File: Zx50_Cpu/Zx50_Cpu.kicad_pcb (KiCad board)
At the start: 4 copper layers, 139.2 x 100.3 mm, 24 parts, among them J1 Zx50_EdgeConnector, J2 FrontPanelConnect, J3 Clock Mezzanine, J4 Front Panel, SW1 RESET, U1 74AHC1G14, U2 SN74AHCT245N, U3 SN74AHCT245N, U4 Z84C00xxP, U5 SN74AHCT245N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

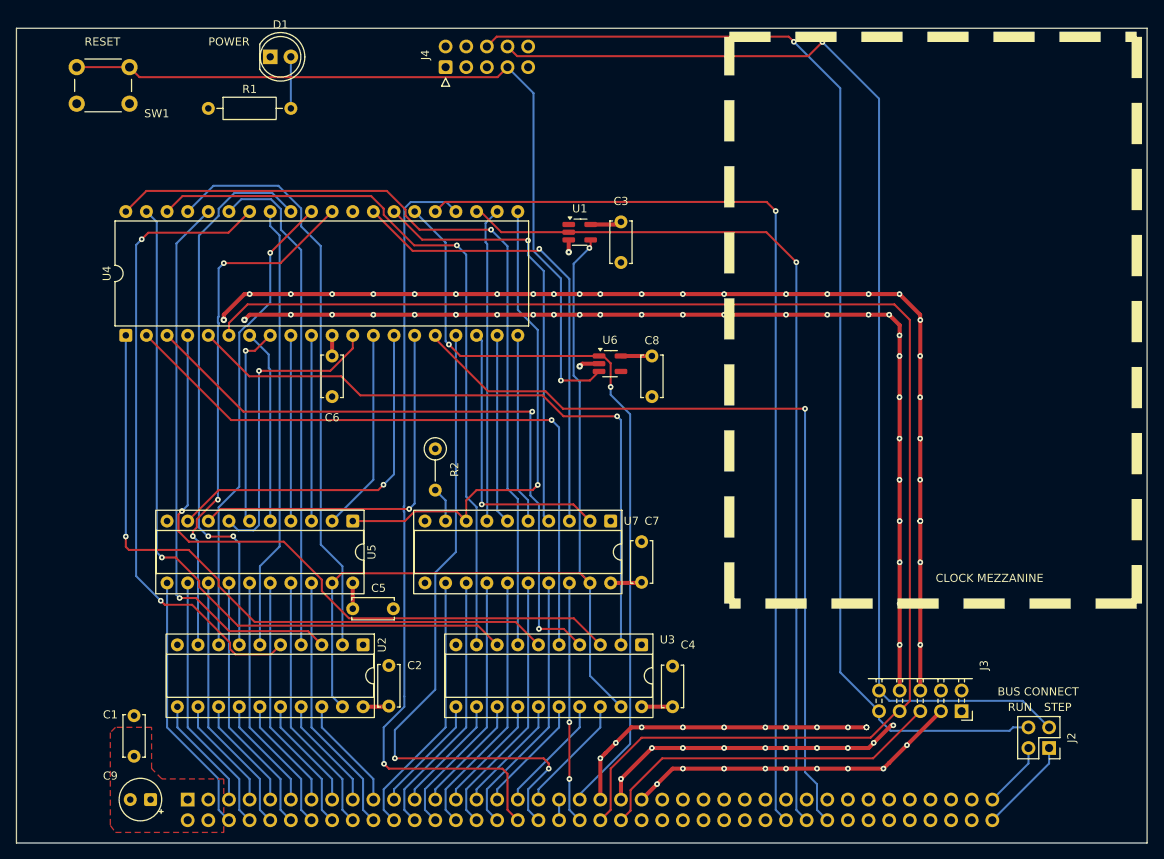
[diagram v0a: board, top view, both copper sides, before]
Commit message: add mounting holes
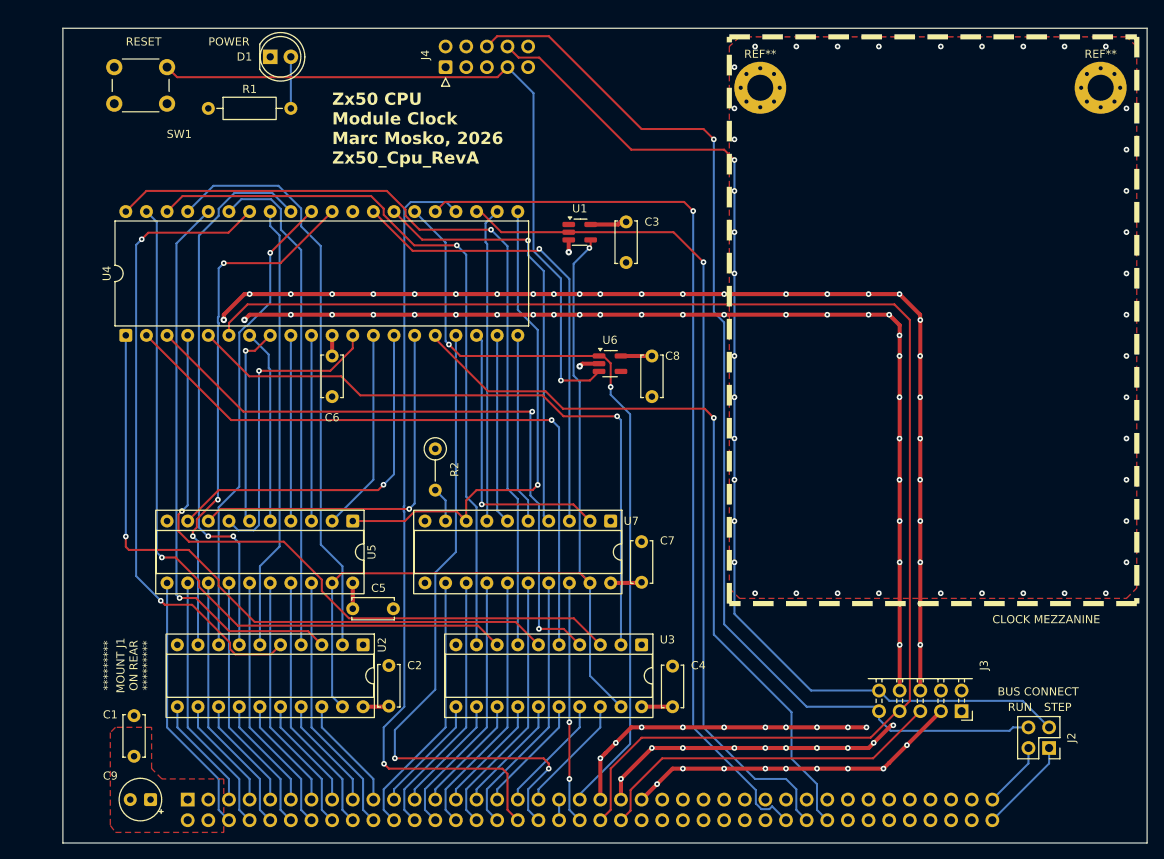
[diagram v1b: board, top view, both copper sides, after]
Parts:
- added REF**: MountingHole_3.2mm_M3_Pad_Via, MountingHole:MountingHole_3.2mm_M3_Pad_Via, F.Cu at (153.0, 71.1)
- added REF**: MountingHole_3.2mm_M3_Pad_Via, MountingHole:MountingHole_3.2mm_M3_Pad_Via, F.Cu at (111.1, 71.1)
- moved SW1 4.62 mm to (31.6, 68.6)
- moved C3 0.63 mm to (94.6, 87.6)
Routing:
- net /~STEP: track 145.5 -> 134.1 mm
- net /~RESET_SW: track 100.5 -> 89.4 mm
- net /RUN: track 145.5 -> 137.6 mm
- net /~INT~: track 100.9 -> 93.6 mm
- net /~BUSRQ~: track 118.4 -> 113.7 mm
- net /~BUSAK~: track 110.7 -> 106.2 mm
- net +5V: track 23.6 -> 24.7 mm
- net /~RESET~: track 95.7 -> 95.1 mm
- net GND: vias 89 -> 128
- added copper zone on F.Cu, net GND
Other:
- board size 139.2 x 100.3 mm -> 133.5 x 100.3 mm
- board text added: "********* MOUNT J1 ON REAR *********"
- board text added: "Zx50 CPU Module Clock Marc Mosko, 2026 Zx50_Cpu_RevA"

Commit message: finish up cpu card, begin on serial card.
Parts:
- moved C8 1.42 mm to (98.4, 102.9)
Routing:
- net /~BUSRQ~: track 113.7 -> 112.4 mm
- net /~INT~: track 93.6 -> 92.5 mm
- net /~STEP: track 134.1 -> 133.0 mm
- net +5V: track 24.7 -> 25.2 mm
- net GND: vias 128 -> 119
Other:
- board text added: "Zx50 CPU Modular Clock Marc Mosko, 2026 Zx50_Cpu_RevA.7"
- board text removed: "Zx50 CPU Module Clock Marc Mosko, 2026 Zx50_Cpu_RevA"
